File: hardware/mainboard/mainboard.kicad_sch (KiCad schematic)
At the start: 130 parts, among them J1 MAINS 4P, J10 AudioJack3, J11 AudioJack3, J12 AudioJack3, J13 AudioJack3, J2 AudioJack3, J3 AudioJack3, J4 AudioJack3, J5 AudioJack3, J6 AudioJack3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

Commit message: hw: Create PCB layout (missing power section)
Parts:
- removed C10, C11, C12, C13, C14, C15, C16, C5, C6, C7, C8, C9: 33nF, symbol Device:C
- removed C17, C23, C29, C35: 100nf, symbol Device:C_Small
- removed C18, C24, C30, C33, C36, C39, C46, C48: 10uF, symbol Device:C_Small
- removed C19, C26, C32, C38: 4.7uF, symbol Device:C_Small
- removed C2, C3, C4: 33nF 50V, symbol Device:C
- removed C20, C21, C22, C25, C27, C28, C31, C34, C37, C40, C45, C47: 100nF, symbol Device:C_Small
- removed C41: 470uF 6.3V, symbol Device:C_Polarized_Small
- removed F1, F2, F3: 250mA 250VAC SB, symbol Device:Fuse_Small
- removed J1: MAINS 4P, symbol Connector:Screw_Terminal_01x04
- removed J10, J11, J12, J13, J2, J3, J4, J5, J6, J7, J8, J9: AudioJack3, symbol Connector_Audio:AudioJack3
- removed R1, R11, R12, R13, R14, R2, R3, R4, R6, R7, R8, R9: 330K, symbol Device:R
- removed R10, R15, R5: 1K, symbol Device:R
- removed R16, R17, R18, R19, R20, R21, R22, R23, R24, R25, R26, R27, R28, R29, R30, R31, R32, R33, R34, R35, R36, R37, R38, R39: 1k, symbol Device:R
- removed R40, R41, R42, R43: 10k, symbol Device:R
- removed R46, R47, R48: 33R 1W, symbol Device:R_Small
- removed R49: 1M 0.5W, symbol Device:R_Small
- removed U1, U2, U3, U4: ATM90E32AS-AU-R, ATM90E32AS-AU-R:QFP50P900X900X120-48N, symbol ATM90E32AS-AU-R:ATM90E32AS-AU-R
- removed Y1, Y2, Y3, Y4: 16.384MHz, symbol Device:Crystal_Small
- added C4: 22uf 10V, Capacitor_SMD:C_1206_3216Metric_Pad1.33x1.80mm_HandSolder, symbol Device:C_Small
- added D4: SMCJ400CA, Diode_SMD:D_SMC_Handsoldering, symbol Device:D_TVS
- added J1: MAINS (MSTBA 5.08mm), Connector_Phoenix_GMSTB:PhoenixContact_GMSTBA_2,5_4-G-7,62_1x04_P7.62mm_Horizontal, symbol Connector:Conn_01x04_Pin
- added J14: Conn_02x03_Odd_Even, Connector_PinHeader_2.54mm:PinHeader_2x03_P2.54mm_Vertical, symbol Connector_Generic:Conn_02x03_Odd_Even
- added R1, R2, R3: 33R 1W Fusible, Resistor_THT:R_Axial_DIN0411_L9.9mm_D3.6mm_P12.70mm_Horizontal, symbol Device:R_Small
- added R4, R5: 500k, Resistor_SMD:R_1206_3216Metric_Pad1.30x1.75mm_HandSolder, symbol Device:R_Small
- added TP1, TP10, TP2, TP3, TP4, TP5, TP6, TP7, TP8, TP9: TestPoint, TestPoint:TestPoint_Pad_1.0x1.0mm, symbol Connector:TestPoint
- C1: value 100uF 400V -> 10uF 450V; footprint (none) -> Capacitor_THT:CP_Radial_D10.0mm_P5.00mm
- C2: renamed from C44; value 100nF 630V -> 100nF 450V; footprint (none) -> Capacitor_THT:C_Rect_L13.0mm_W4.0mm_P10.00mm_FKS3_FKP3_MKS4
- C3: renamed from C43; footprint (none) -> Capacitor_SMD:C_0603_1608Metric_Pad1.08x0.95mm_HandSolder
- C5: renamed from C42; footprint (none) -> Capacitor_SMD:C_0603_1608Metric_Pad1.08x0.95mm_HandSolder
- D1: renamed from D3; footprint (none) -> Diode_SMD:D_SMA_Handsoldering
- D2: footprint (none) -> Diode_SMD:D_SMA_Handsoldering
- D3: renamed from D1; footprint (none) -> Diode_SMD:D_SMA_Handsoldering
- R6: renamed from R45; footprint (none) -> Resistor_SMD:R_0603_1608Metric_Pad0.98x0.95mm_HandSolder
- R7: renamed from R44; footprint (none) -> Resistor_SMD:R_0603_1608Metric_Pad0.98x0.95mm_HandSolder
- RV1, RV2, RV3: value 275VAC MOV -> MOV-10D431K; footprint (none) -> Varistor:RV_Disc_D12mm_W5.4mm_P7.5mm
- SW1, SW2: footprint (none) -> Button_Switch_THT:SW_Tactile_SPST_Angled_PTS645Vx31-2LFS
- renumbered U5 to U1
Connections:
- net +3V3: now also C4.1, J14.2 (Pin_2)
- net CS_1: now also TP4.1
- net CS_2: now also TP5.1
- net CS_3: now also TP6.1
- net CS_4: now also TP7.1
- net HV_DC: now also D4.2 (A2), R4.1
- net L1: now also D3.2 (A), RV3.2, R3.2
- net L2: now also D2.2 (A), RV2.2, R2.2
- net L3: now also D1.2 (A), RV1.2, R1.2
- net SPI_MISO: now also U1.9 (IO16), TP2.1; no longer U1.5 (IO5)
- net SPI_MOSI: now also U1.8 (IO15), TP1.1; no longer U1.4 (IO4)
- net SPI_SCK: now also U1.10 (IO17), TP3.1; no longer U1.6 (IO6)
- net IO0: now reaches R7.2, SW2.2, U1.27 (IO0)
- net IO0: now also J14.6 (Pin_6)
- net EN: now reaches C3.2, R6.2, SW1.2, U1.3 (EN)
- net EN: now also J14.4 (Pin_4)
- net at U1.36 (RXD0): now also J14.5 (Pin_5)
- net at U1.37 (TXD0): now also J14.3 (Pin_3)
- net AGND renamed GND
- net GND: now also C4.2, D4.1 (A1), J1.1 (Pin_1), J14.1 (Pin_1), R5.2
- new net: R4.2, R5.1
- new net: J1.4 (Pin_4), R3.1
- new net: J1.3 (Pin_3), R2.1
- new net: J1.2 (Pin_2), R1.1
- new net metering_block/V1P_IN: TP8.1
- new net metering_block/V2P_IN: TP9.1
- new net metering_block/V3P_IN: TP10.1
- no-connect marks 68 -> 26
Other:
- added sheet metering_block (metering_block.kicad_sch)
- added sheet metering_block1 (metering_block.kicad_sch)
- added sheet metering_block2 (metering_block.kicad_sch)
- added sheet metering_block3 (metering_block.kicad_sch)
- added sheet voltage_divider (voltage_divider.kicad_sch)
- added sheet voltage_divider1 (voltage_divider.kicad_sch)
- added sheet voltage_divider2 (voltage_divider.kicad_sch)
- moved on the sheet: C1, C2, C3, C5, D1, D2, D3, R6, R7, RV1, RV2, RV3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

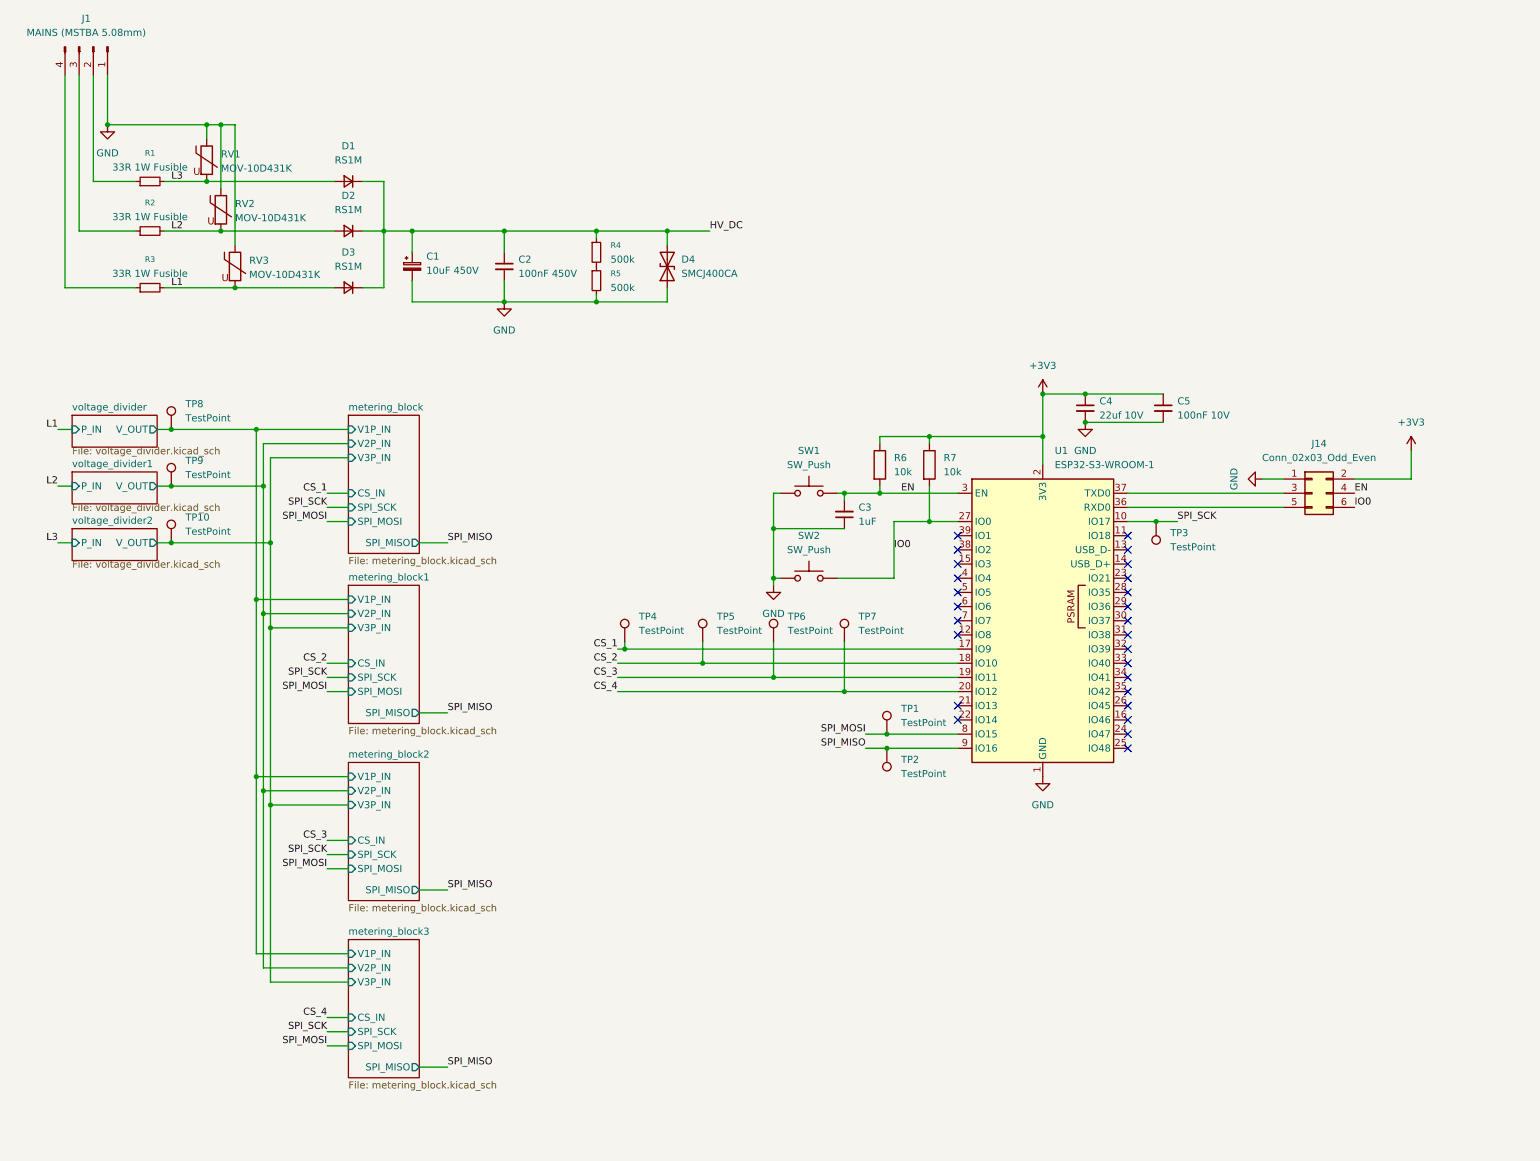
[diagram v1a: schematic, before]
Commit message: hw: Add 5V buck regulator
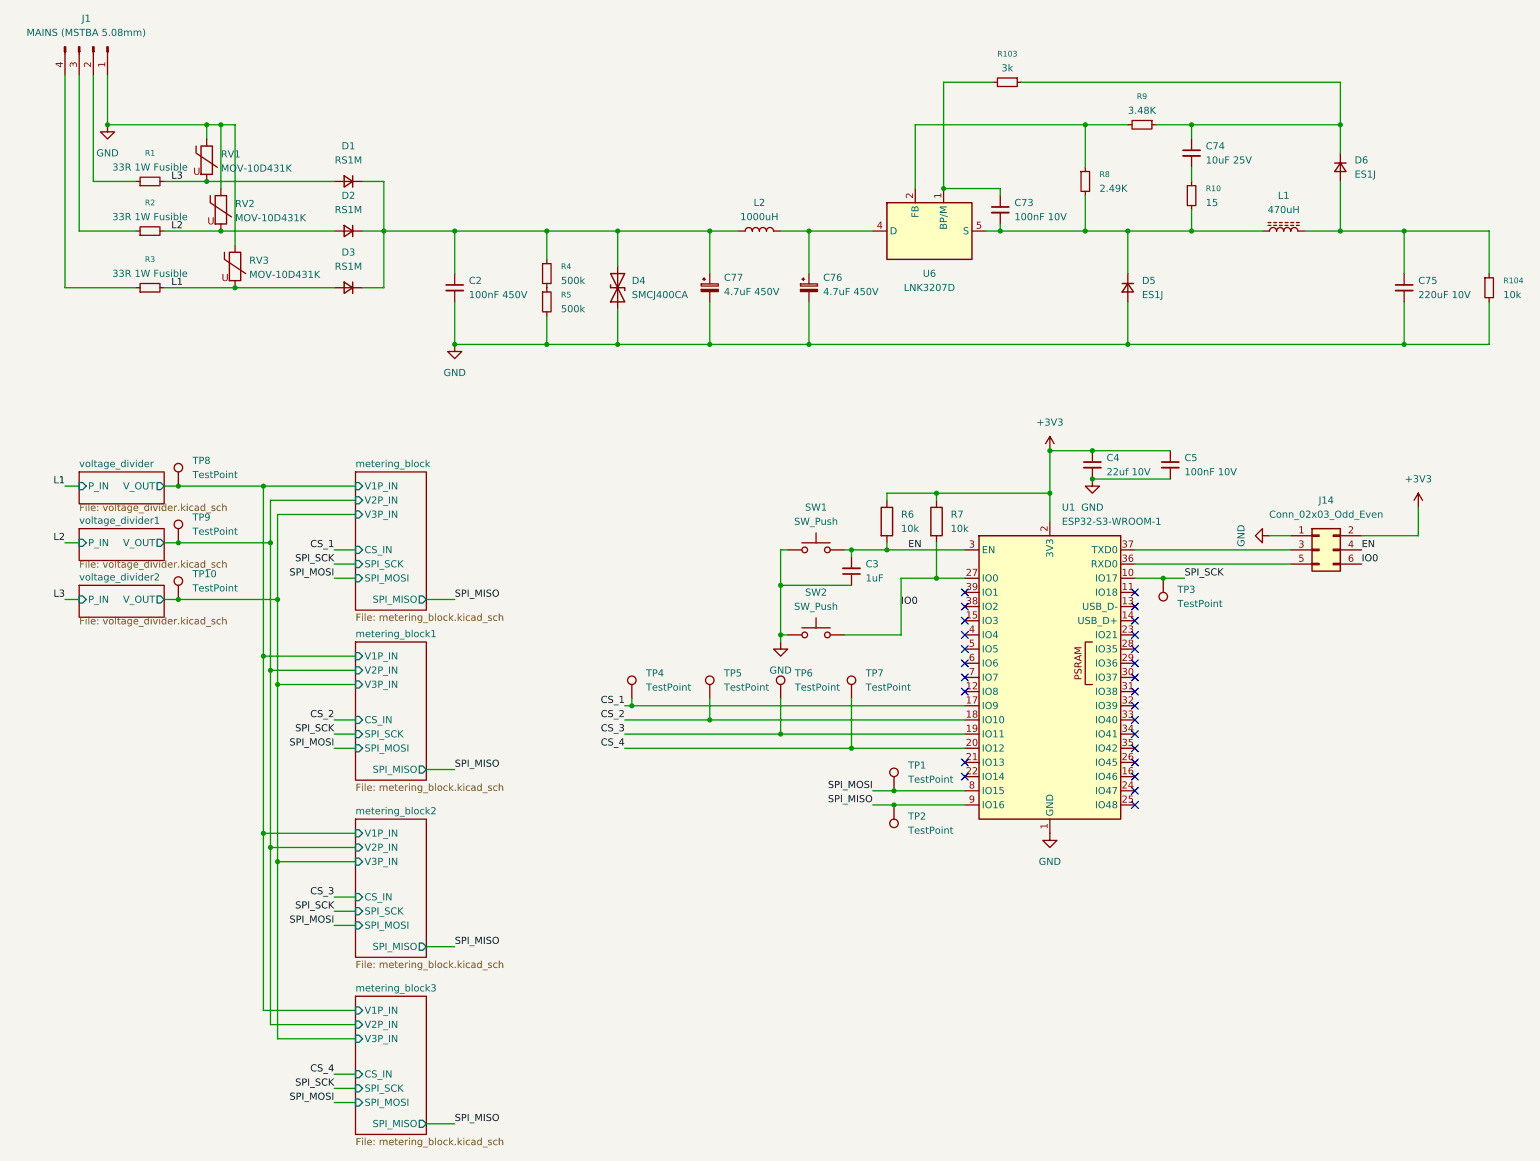
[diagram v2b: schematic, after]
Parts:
- removed C1: 10uF 450V, Capacitor_THT:CP_Radial_D10.0mm_P5.00mm, symbol Device:C_Polarized_Small
- added C73: 100nF 10V, Capacitor_SMD:C_0603_1608Metric_Pad1.08x0.95mm_HandSolder, symbol Device:C_Small
- added C74: 10uF 25V, Capacitor_SMD:C_0805_2012Metric_Pad1.18x1.45mm_HandSolder, symbol Device:C_Small
- added C75: 220uF 10V, Capacitor_THT:CP_Radial_D6.3mm_P2.50mm, symbol Device:C_Small
- added C76, C77: 4.7uF 450V, Capacitor_THT:CP_Radial_D10.0mm_P5.00mm, symbol Device:C_Polarized_Small
- added D5, D6: ES1J, Diode_SMD:D_SMA_Handsoldering, symbol Device:D_Small
- added L1: 470uH, Inductor_SMD:L_Bourns_SRR1208_12.7x12.7mm, symbol Device:L_Ferrite
- added L2: 1000uH, Inductor_SMD:L_6.3x6.3_H3, symbol Device:L
- added R10: 15, Resistor_SMD:R_0603_1608Metric_Pad0.98x0.95mm_HandSolder, symbol Device:R_Small
- added R103: 3k, Resistor_SMD:R_0603_1608Metric_Pad0.98x0.95mm_HandSolder, symbol Device:R_Small
- added R104: 10k, Resistor_SMD:R_0603_1608Metric_Pad0.98x0.95mm_HandSolder, symbol Device:R_Small
- added R8: 2.49K, Resistor_SMD:R_0603_1608Metric_Pad0.98x0.95mm_HandSolder, symbol Device:R_Small
- added R9: 3.48K, Resistor_SMD:R_0603_1608Metric_Pad0.98x0.95mm_HandSolder, symbol Device:R_Small
- added U6: LNK3207D, Package_SO:PowerIntegrations_SO-8C, symbol Regulator_Switching:LNK3206D
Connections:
- net GND: now also C75.2, C76.2, C77.2, D5.2 (A), R104.2
- net HV_DC: no longer names the net of C2.1, D1.1 (K), D2.1 (K), D3.1 (K), D4.2 (A2), R4.1
- net HV_DC: now also C77.1, L2.1
- new net: C76.1, L2.2, U6.4 (D)
- new net: C74.2, R10.1
- new net: C73.2, D5.1 (K), L1.1, R10.2, R8.2, U6.5 (S), U6.6 (S), U6.7 (S), U6.8 (S)
- new net: C74.1, D6.1 (K), R103.1, R9.1
- new net: R8.1, R9.2, U6.2 (FB)
- new net: C75.1, D6.2 (A), L1.2, R104.1
- new net: C73.1, R103.2, U6.1 (BP/M)
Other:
- moved on the sheet: C2, C3, C4, C5, D4, J14, R4, R5, R6, R7, SW1, SW2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

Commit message: hw: Redo HV section layout
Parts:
- removed D4: SMCJ400CA, Diode_SMD:D_SMC_Handsoldering, symbol Device:D_TVS
- added C78: 10uF, Capacitor_SMD:C_0805_2012Metric_Pad1.18x1.45mm_HandSolder, symbol Device:C_Small
- added C79: 22uF, Capacitor_SMD:C_0805_2012Metric_Pad1.18x1.45mm_HandSolder, symbol Device:C_Small
- added D4: TPSMB440A-A, Diode_SMD:D_SMB_Handsoldering, symbol Device:D_Zener
- added L3: 1000uH, Inductor_SMD:L_6.3x6.3_H3, symbol Device:L
- added U7: AMS1117-3.3, Package_TO_SOT_SMD:SOT-223-3_TabPin2, symbol Regulator_Linear:AMS1117-3.3
- SW1, SW2: footprint Button_Switch_THT:SW_Tactile_SPST_Angled_PTS645Vx31-2LFS -> Button_Switch_THT:SW_Tactile_SPST_Angled_PTS645Vx58-2LFS
- TP10: value TestPoint -> V3
- TP8: value TestPoint -> V1
- TP9: value TestPoint -> V2
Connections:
- net +3V3: now also C79.1, U7.2 (VO)
- net GND: now also C78.2, C79.2, D4.2 (A), U7.1 (GND)
- net L1: now also D1.2 (A), R1.2, RV1.2; no longer D3.2 (A), R3.2, RV3.2
- net L3: now also D3.2 (A), R3.2, RV3.2; no longer D1.2 (A), R1.2, RV1.2
- net metering_block/V1P_IN: now also TP10.1; no longer TP8.1
- net metering_block/V3P_IN: now also TP8.1; no longer TP10.1
- net at C2.1, C77.1, L2.1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: now also D4.1 (K), L3.2; no longer D1.1 (K), D2.1 (K), D3.1 (K)
- net at C75.1, D6.2 (A), L1.2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: now also C78.1, U7.3 (VI)
- net at R3.1: now also J1.2 (Pin_2); no longer J1.4 (Pin_4)
- net at R1.1: now also J1.4 (Pin_4); no longer J1.2 (Pin_2)
- new net: D1.1 (K), D2.1 (K), D3.1 (K), L3.1
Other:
- moved on the sheet: D1, D3, R1, R3, RV1, RV3, TP10, TP8

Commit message: hw: Add LDO and GND/3V3 traces
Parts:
- removed TP1, TP2, TP3, TP4, TP5, TP6, TP7: TestPoint, TestPoint:TestPoint_Pad_1.0x1.0mm, symbol Connector:TestPoint
- removed TP10: V3, TestPoint:TestPoint_Pad_1.0x1.0mm, symbol Connector:TestPoint
- removed TP8: V1, TestPoint:TestPoint_Pad_1.0x1.0mm, symbol Connector:TestPoint
- removed TP9: V2, TestPoint:TestPoint_Pad_1.0x1.0mm, symbol Connector:TestPoint

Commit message: hw: Complete final(?) board design
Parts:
- added J15: Conn_02x02_Odd_Even, Connector_PinHeader_2.54mm:PinHeader_2x02_P2.54mm_Vertical, symbol Connector_Generic:Conn_02x02_Odd_Even
- added TP1: V1, TestPoint:TestPoint_Pad_1.0x1.0mm, symbol Connector:TestPoint
- added TP10: MISO, TestPoint:TestPoint_Pad_1.0x1.0mm, symbol Connector:TestPoint
- added TP11: 5V, TestPoint:TestPoint_Pad_1.0x1.0mm, symbol Connector:TestPoint
- added TP2: V2, TestPoint:TestPoint_Pad_1.0x1.0mm, symbol Connector:TestPoint
- added TP3: V3, TestPoint:TestPoint_Pad_1.0x1.0mm, symbol Connector:TestPoint
- added TP4: CS1, TestPoint:TestPoint_Pad_1.0x1.0mm, symbol Connector:TestPoint
- added TP5: CS2, TestPoint:TestPoint_Pad_1.0x1.0mm, symbol Connector:TestPoint
- added TP6: CS3, TestPoint:TestPoint_Pad_1.0x1.0mm, symbol Connector:TestPoint
- added TP7: CS4, TestPoint:TestPoint_Pad_1.0x1.0mm, symbol Connector:TestPoint
- added TP8: SCK, TestPoint:TestPoint_Pad_1.0x1.0mm, symbol Connector:TestPoint
- added TP9: MOSI, TestPoint:TestPoint_Pad_1.0x1.0mm, symbol Connector:TestPoint
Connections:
- net +3V3: now also J15.2 (Pin_2), J15.4 (Pin_4); no longer C79.1, U7.2 (VO)
- net CS_1: now also TP4.1
- net CS_2: now also TP5.1
- net CS_3: now also TP6.1
- net CS_4: now also TP7.1
- net SPI_MISO: now also TP10.1
- net SPI_MOSI: now also TP9.1
- net SPI_SCK: now also TP8.1
- net metering_block/V1P_IN: now also TP1.1
- net metering_block/V2P_IN: now also TP2.1
- net metering_block/V3P_IN: now also TP3.1
- net at C75.1, C78.1, D6.2 (A)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: now also TP11.1
- new net: C79.1, J15.1 (Pin_1), J15.3 (Pin_3), U7.2 (VO)
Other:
- note added: "GND CONNECTED TO MAINS NEUTRAL!"
- moved on the sheet: C76, C77, L2
